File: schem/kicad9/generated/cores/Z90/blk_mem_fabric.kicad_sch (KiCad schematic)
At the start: 0 parts

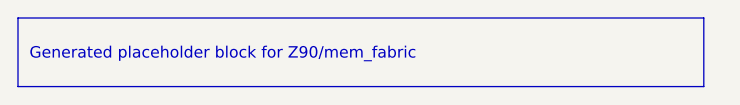
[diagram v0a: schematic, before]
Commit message: kicad: generate core-level hierarchical schematics
Detailed description:
- What changed: regenerated common and core schematics for Z85/Z90/Z380/Z480, Am9513/4/5, Am95xx, and CarbonIO/DMA placeholders
- Why it changed: update generated KiCad 9 outputs to reflect the final naming and tier model
- Files/paths affected: schem/kicad9/generated/common/* and schem/kicad9/generated/cores/*
- How to run it: scripts/gen_kicad.sh (or python tools/kicadgen/src/kicadgen.py)
- What remains TODO: regenerate and commit system-level schematics
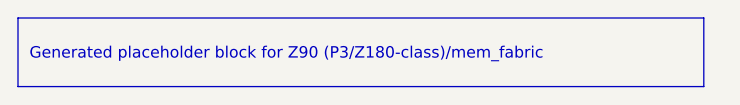
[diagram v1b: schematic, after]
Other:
- title: Z90::mem_fabric -> Z90 (P3/Z180-class)::mem_fabric
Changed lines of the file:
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@@
 	(version 20250114)
 	(generator "kicadgen")
-	(generator_version "0.1")
+	(generator_version "0.2")
 	(paper "A3")
 	(title_block
-		(title "Z90::mem_fabric")
+		(title "Z90 (P3/Z180-class)::mem_fabric")
 		(company "Project Carbon")
 		(comment 1 "Generated - do not edit in generated/")
@@
 	)
 	(text_box
-		"Generated placeholder block for Z90/mem_fabric"
+		"Generated placeholder block for Z90 (P3/Z180-class)/mem_fabric"
 		(exclude_from_sim no)
 		(at
